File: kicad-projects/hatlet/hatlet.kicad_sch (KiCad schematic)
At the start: 51 parts, among them J1 Racklet_USBHeader_02x06, J2 SWD, J3 PMOD0, J4 PMOD2, J5 PMOD1, J6 UART0, J7 PMOD3, SW1 BOOTSEL, SW2 RESET, U1 AMS1117-3.3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

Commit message: wip: check in progress
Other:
- note added: "TODO: - Add button"
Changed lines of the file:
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@@
+    (effects (font (size 1.27 1.27)) (justify left bottom))
+  )
+  (text "TODO:\n- Add button" (at 25.4 130.81 0)
     (effects (font (size 1.27 1.27)) (justify left bottom))
   )

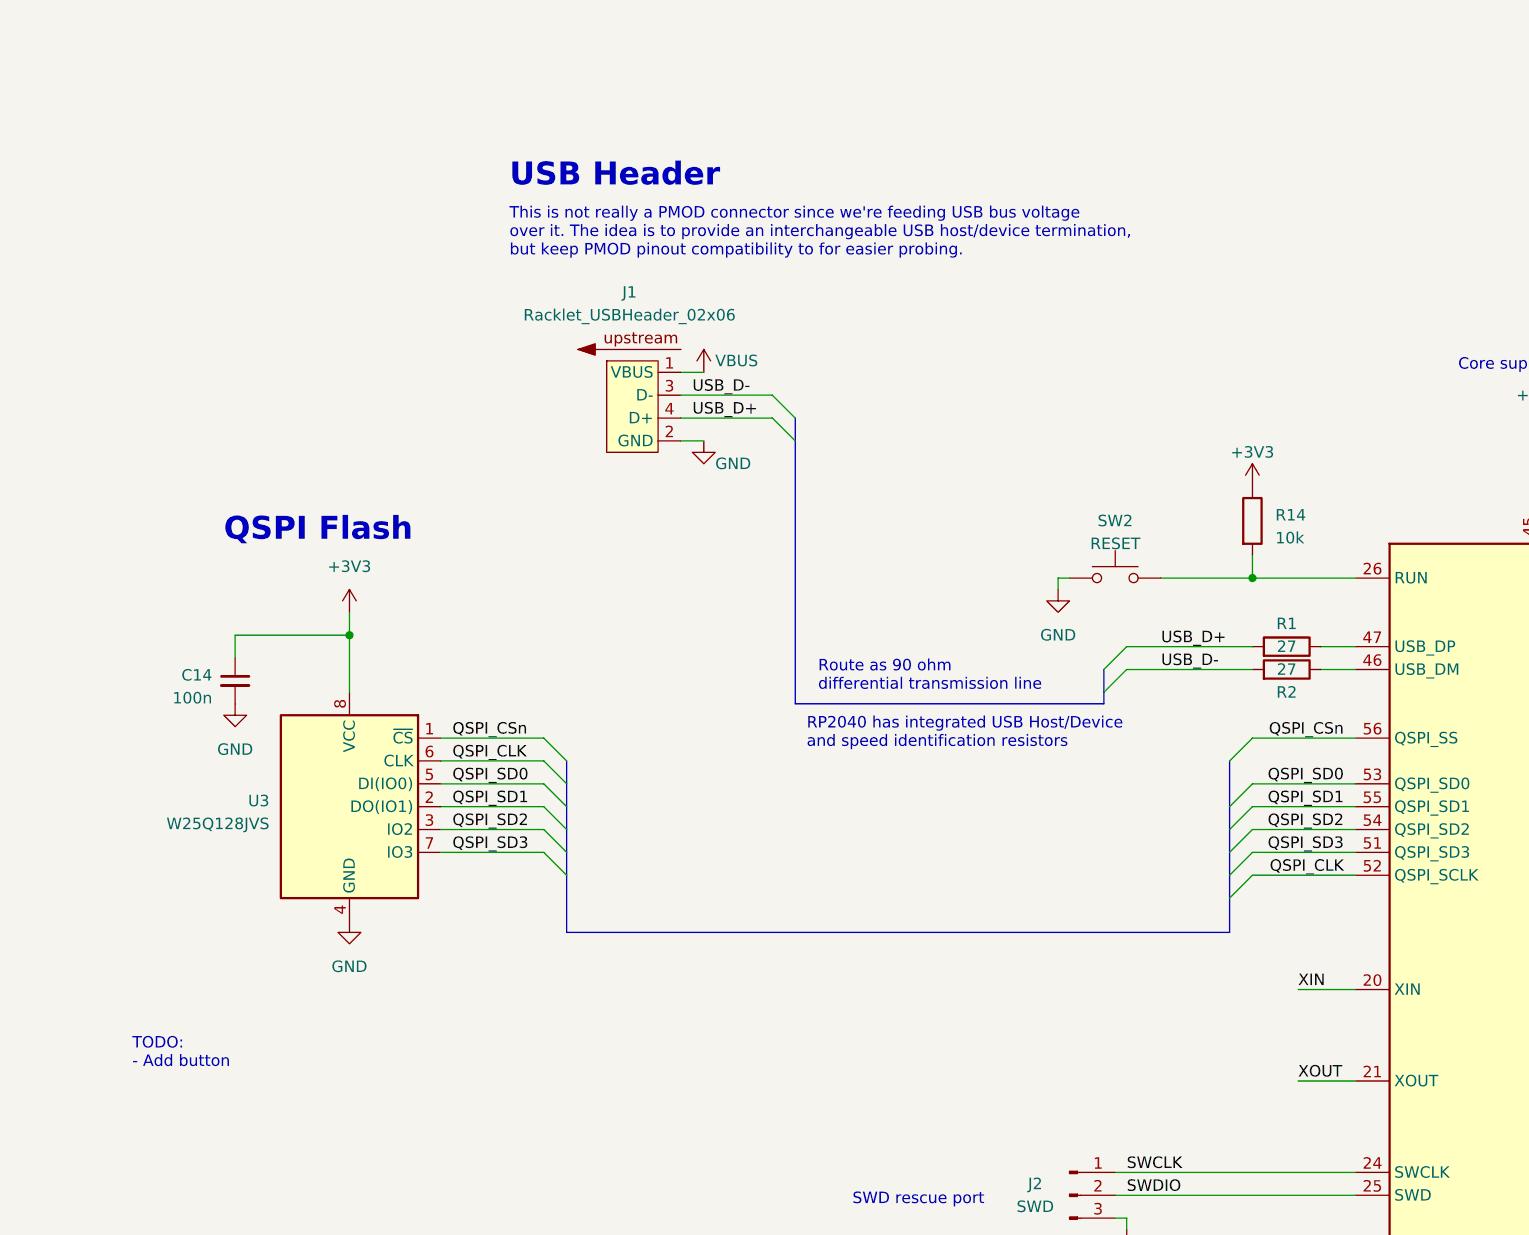
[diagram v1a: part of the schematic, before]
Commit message: hatlet: replace USBHeader with BackplaneHeader
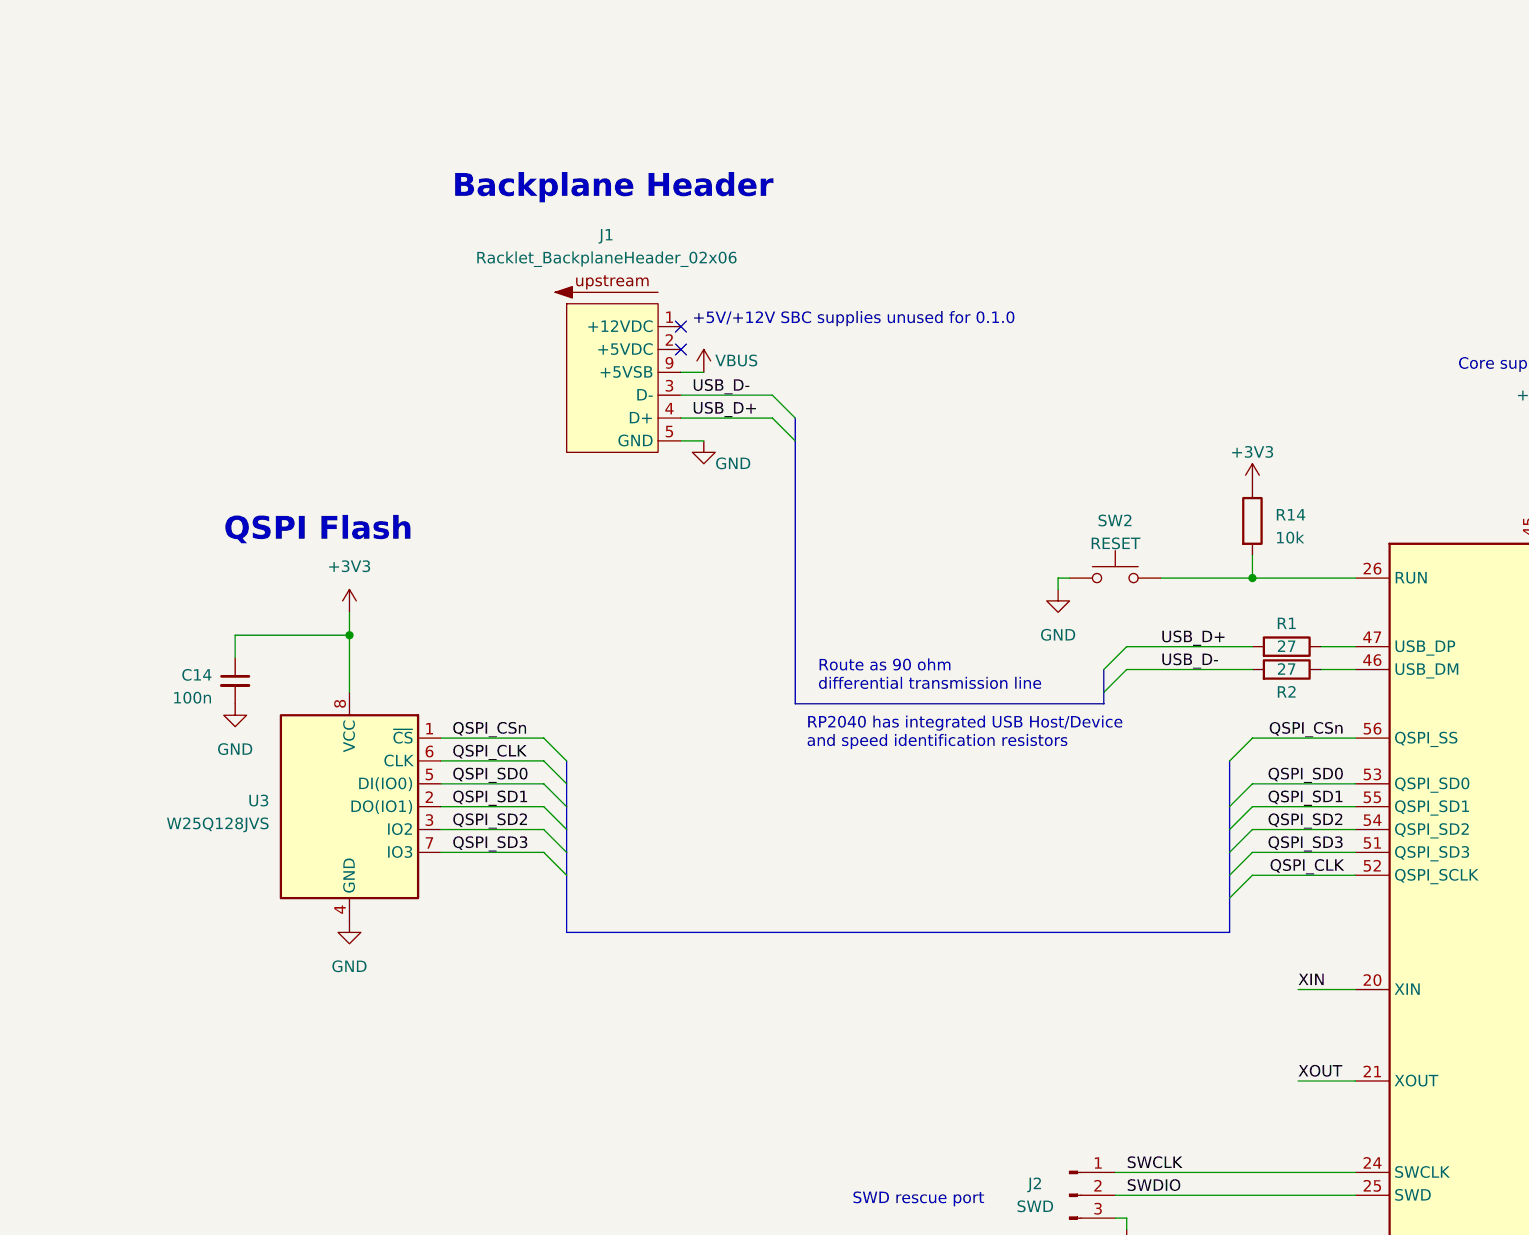
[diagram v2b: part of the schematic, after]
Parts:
- removed J1: Racklet_USBHeader_02x06, racklet:Racklet_USBHeader_02x06, symbol racklet:Racklet_USBHeader_02x06
- added J1: Racklet_BackplaneHeader_02x06, racklet:Racklet_BackplaneHeader_02x06, symbol racklet:Racklet_BackplaneHeader_02x06
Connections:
- net GND: now also J1.10 (GND), J1.11 (GND), J1.12 (GND), J1.5 (GND), J1.6 (GND)
- net USB_D+: now also J1.4 (D+)
- net USB_D-: now also J1.3 (D-)
- net VBUS: now also J1.9 (+5VSB)
- new net +12VDC: J1.1 (+12VDC), J1.7 (+12VDC)
- new net +5VDC: J1.2 (+5VDC), J1.8 (+5VDC)
- no-connect marks 4 -> 6
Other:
- note added: "+5V/+12V SBC supplies unused for ${REVISION}"
- note added: "Backplane Header"
- note removed: "TODO: - Add button"
- note removed: "This is not really a PMOD connector since we're feeding USB bus voltage over it. The idea is to provide an interchangeable USB host/device termination, but keep PMOD pinout compatibility to for easier probing."
- note removed: "USB Header"
